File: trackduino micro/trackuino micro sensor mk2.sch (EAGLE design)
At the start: 42 parts, among them IC2 74AHC1G125DBV, SW1 SPST_TACT-KMR2, U1 ATMEGA168MLF, Y1 16MHZ

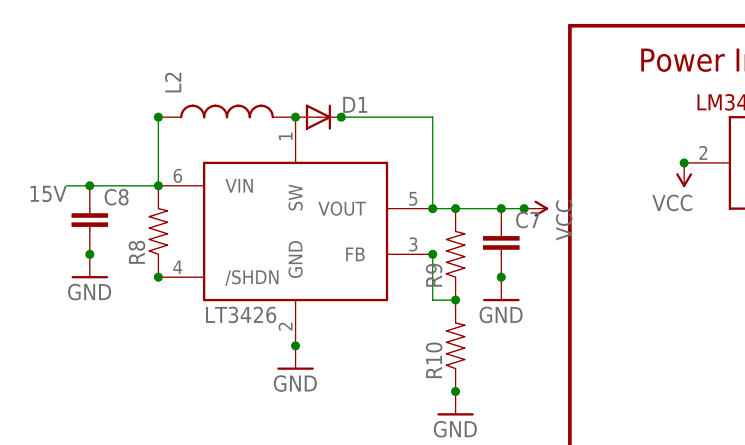
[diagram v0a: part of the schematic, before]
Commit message: sensor mk2 fixes
fixed a short on the boost output and serial RX
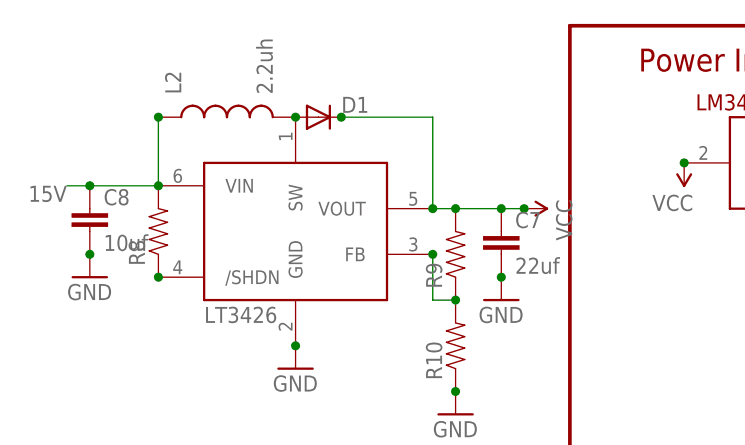
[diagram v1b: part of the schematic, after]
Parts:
- C7: value (none) -> 22uf
- C8: value (none) -> 10uf
- L2: value (none) -> 2.2uh
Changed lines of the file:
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@@
 <part name="U$7" library="adafruit" deviceset="LT3426" device=""/>
 <part name="D1" library="diode" deviceset="DIODE-" device="SOD123"/>
-<part name="L2" library="SparkFun-Passives" deviceset="INDUCTOR" device="0805"/>
+<part name="L2" library="SparkFun-Passives" deviceset="INDUCTOR" device="0805" value="2.2uh"/>
 <part name="R8" library="SparkFun-Resistors" deviceset="RESISTOR" device="0805-RES"/>
 <part name="R9" library="SparkFun-Resistors" deviceset="RESISTOR" device="0805-RES"/>
 <part name="R10" library="SparkFun-Resistors" deviceset="RESISTOR" device="0805-RES"/>
 <part name="GND28" library="SparkFun-Aesthetics" deviceset="GND" device=""/>
-<part name="C7" library="SparkFun-Capacitors" deviceset="CAP" device="0805"/>
-<part name="C8" library="SparkFun-Capacitors" deviceset="CAP" device="0805"/>
+<part name="C7" library="SparkFun-Capacitors" deviceset="CAP" device="0805" value="22uf"/>
+<part name="C8" library="SparkFun-Capacitors" deviceset="CAP" device="0805" value="10uf"/>
 <part name="GND29" library="SparkFun-Aesthetics" deviceset="GND" device=""/>
 <part name="GND30" library="SparkFun-Aesthetics" deviceset="GND" device=""/>

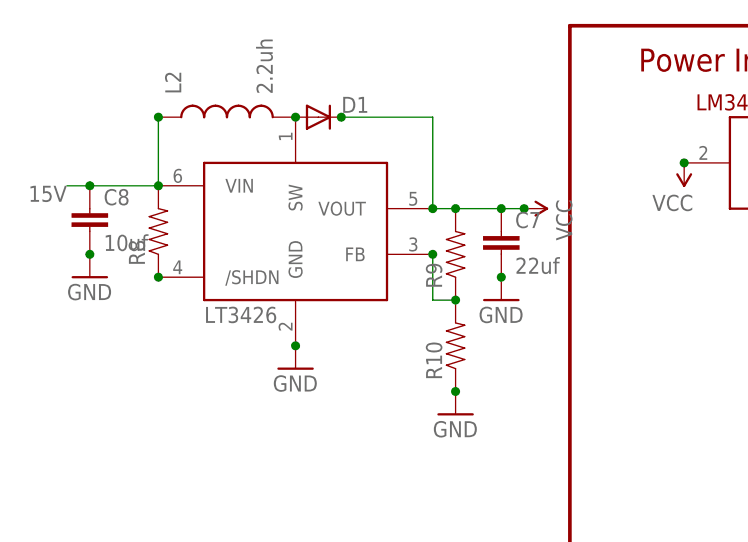
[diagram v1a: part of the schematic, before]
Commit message: DRC check
ran osh park DRC check and resolved errors.
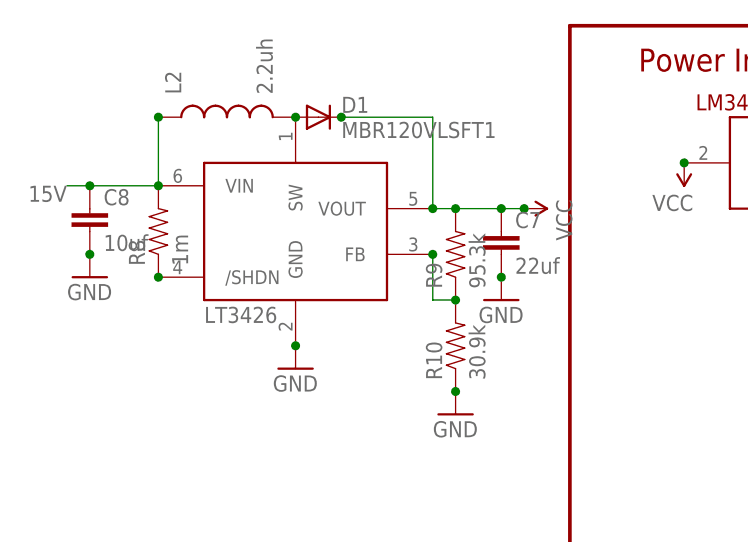
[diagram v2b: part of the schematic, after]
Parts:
- D1: value (none) -> MBR120VLSFT1
- R10: value (none) -> 30.9k
- R8: value (none) -> 1m
- R9: value (none) -> 95.3k
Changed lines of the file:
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@@
 <part name="SUPPLY1" library="SparkFun-Aesthetics" deviceset="VCC" device=""/>
 <part name="U$7" library="adafruit" deviceset="LT3426" device=""/>
-<part name="D1" library="diode" deviceset="DIODE-" device="SOD123"/>
+<part name="D1" library="diode" deviceset="DIODE-" device="SOD123" value="MBR120VLSFT1"/>
 <part name="L2" library="SparkFun-Passives" deviceset="INDUCTOR" device="0805" value="2.2uh"/>
-<part name="R8" library="SparkFun-Resistors" deviceset="RESISTOR" device="0805-RES"/>
-<part name="R9" library="SparkFun-Resistors" deviceset="RESISTOR" device="0805-RES"/>
-<part name="R10" library="SparkFun-Resistors" deviceset="RESISTOR" device="0805-RES"/>
+<part name="R8" library="SparkFun-Resistors" deviceset="RESISTOR" device="0805-RES" value="1m"/>
+<part name="R9" library="SparkFun-Resistors" deviceset="RESISTOR" device="0805-RES" value="95.3k"/>
+<part name="R10" library="SparkFun-Resistors" deviceset="RESISTOR" device="0805-RES" value="30.9k"/>
 <part name="GND28" library="SparkFun-Aesthetics" deviceset="GND" device=""/>
 <part name="C7" library="SparkFun-Capacitors" deviceset="CAP" device="0805" value="22uf"/>

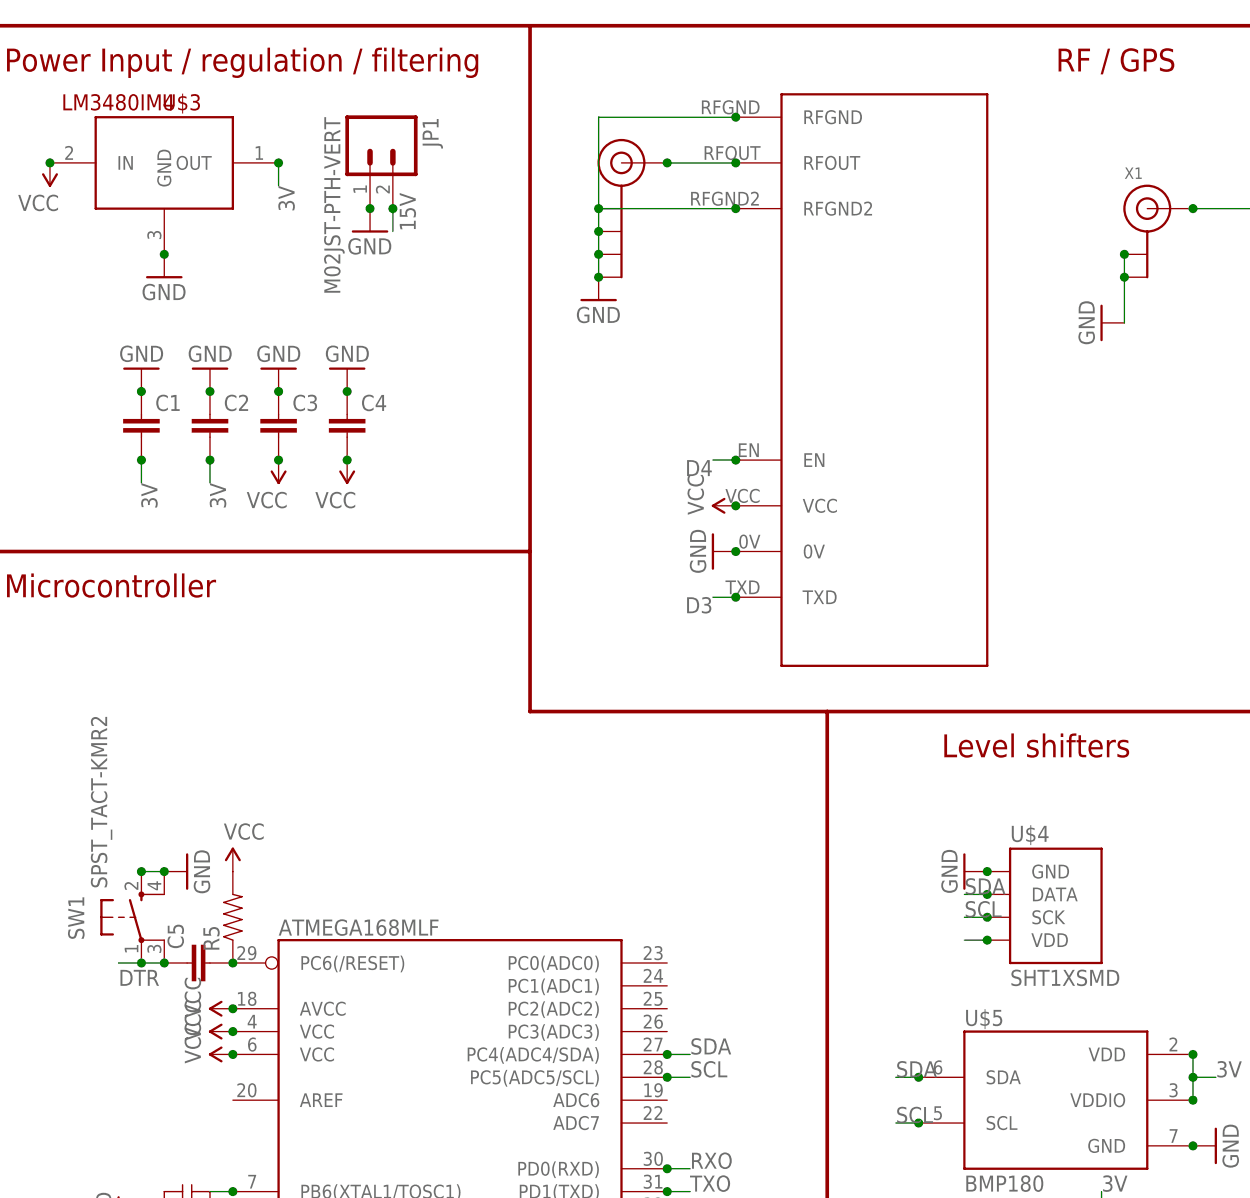
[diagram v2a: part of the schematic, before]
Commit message: boost converter fix
fixed external component placement and added some silkscreen
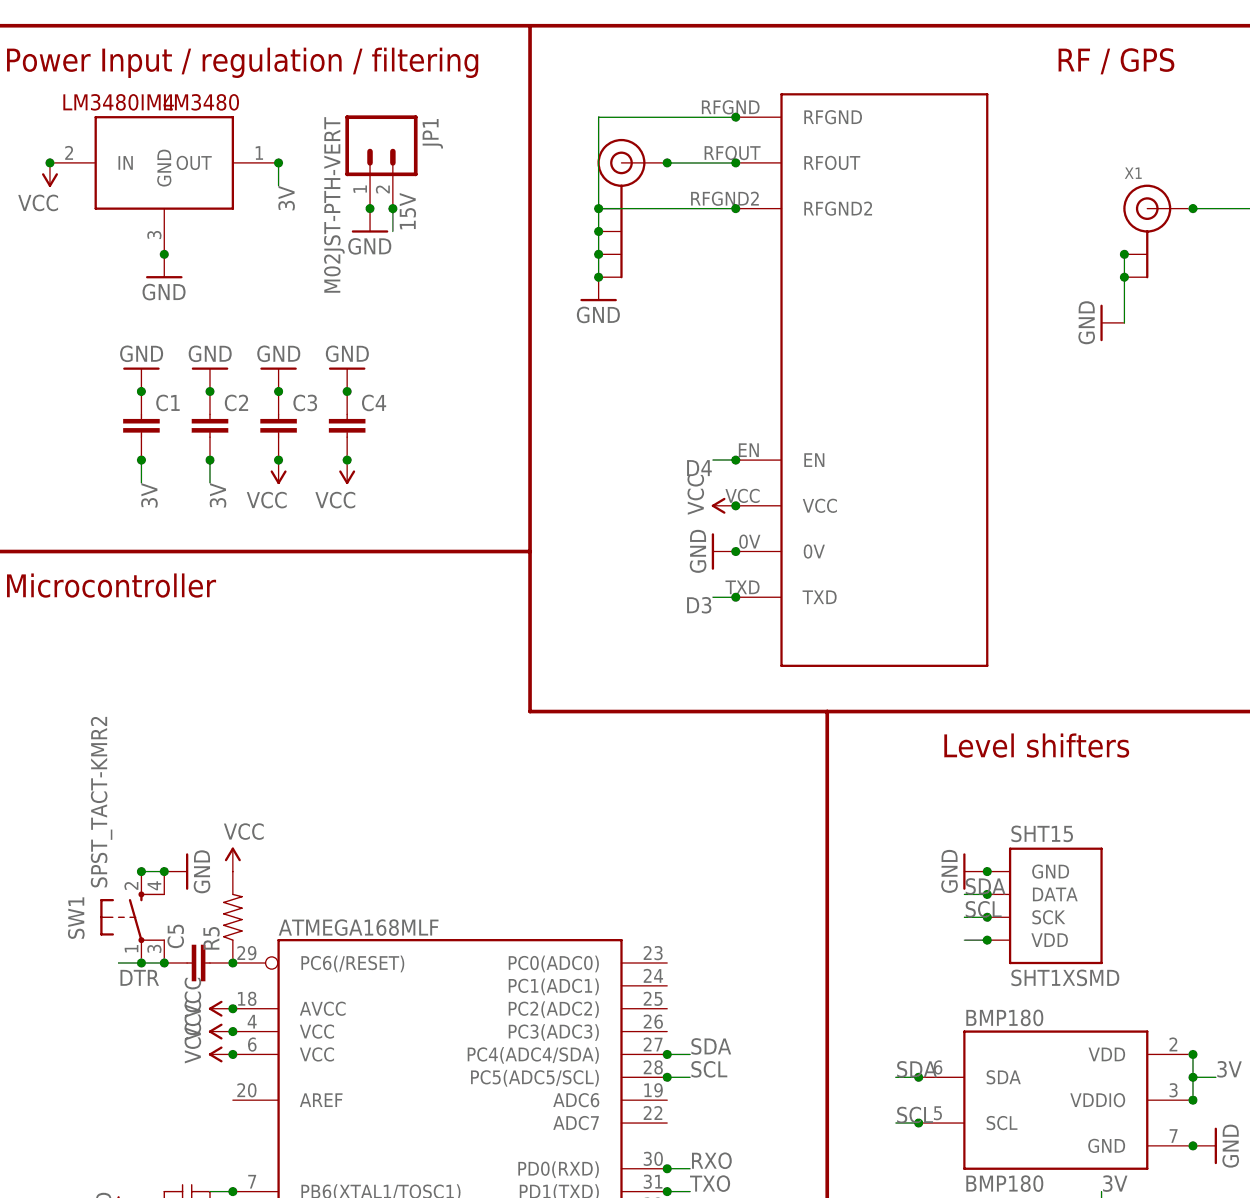
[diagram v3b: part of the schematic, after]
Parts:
- renumbered U$3 to LM3480, U$4 to SHT15, U$5 to BMP180, U$7 to LT3426
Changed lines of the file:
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@@
 <part name="U1" library="SparkFun-DigitalIC" deviceset="ATMEGA168" device="MLF" value="ATMEGA168MLF"/>
 <part name="U$2" library="Ava" deviceset="RADIOMETRIX-HX1" device=""/>
-<part name="U$3" library="SparkFun-PowerIC" deviceset="LM3480IM4" device=""/>
+<part name="LM3480" library="SparkFun-PowerIC" deviceset="LM3480IM4" device=""/>
 <part name="GND2" library="SparkFun-Aesthetics" deviceset="GND" device=""/>
 <part name="JP1" library="SparkFun-Connectors" deviceset="M02" device="JST-PTH-VERT" value="M02JST-PTH-VERT"/>
@@
 <part name="RX" library="SparkFun-Connectors" deviceset="M02" device="PTH" value="RX"/>
 <part name="GND10" library="SparkFun-Aesthetics" deviceset="GND" device=""/>
-<part name="U$4" library="SparkFun-Sensors" deviceset="SHT1X" device="SMD"/>
-<part name="U$5" library="SparkFun-Sensors" deviceset="BMP180" device=""/>
+<part name="SHT15" library="SparkFun-Sensors" deviceset="SHT1X" device="SMD"/>
+<part name="BMP180" library="SparkFun-Sensors" deviceset="BMP180" device=""/>
 <part name="GND16" library="SparkFun-Aesthetics" deviceset="GND" device=""/>
 <part name="GND20" library="SparkFun-Aesthetics" deviceset="GND" device=""/>
@@
 <part name="GND27" library="SparkFun-Aesthetics" deviceset="GND" device=""/>
 <part name="SUPPLY1" library="SparkFun-Aesthetics" deviceset="VCC" device=""/>
-<part name="U$7" library="adafruit" deviceset="LT3426" device=""/>
+<part name="LT3426" library="adafruit" deviceset="LT3426" device=""/>
 <part name="D1" library="diode" deviceset="DIODE-" device="SOD123" value="MBR120VLSFT1"/>
 <part name="L2" library="SparkFun-Passives" deviceset="INDUCTOR" device="0805" value="2.2uh"/>
@@
 <instance part="U1" gate="G$1" x="55.88" y="55.88"/>
 <instance part="U$2" gate="G$1" x="91.44" y="134.62" rot="R270"/>
-<instance part="U$3" gate="G$1" x="25.4" y="170.18"/>
+<instance part="LM3480" gate="G$1" x="25.4" y="170.18"/>
 <instance part="GND2" gate="1" x="114.3" y="43.18" rot="R270"/>
 <instance part="JP1" gate="G$1" x="48.26" y="172.72" rot="R270"/>
@@
 <instance part="RX" gate="G$1" x="231.14" y="83.82"/>
 <instance part="GND10" gate="1" x="208.28" y="58.42" rot="R90"/>
-<instance part="U$4" gate="G$1" x="124.46" y="86.36"/>
-<instance part="U$5" gate="G$1" x="124.46" y="66.04"/>
+<instance part="SHT15" gate="G$1" x="124.46" y="86.36"/>
+<instance part="BMP180" gate="G$1" x="124.46" y="66.04"/>
 <instance part="GND16" gate="1" x="142.24" y="60.96" rot="R90"/>
 <instance part="GND20" gate="1" x="114.3" y="91.44" rot="R270"/>
@@
 <instance part="GND27" gate="1" x="-30.48" y="147.32"/>
 <instance part="SUPPLY1" gate="G$1" x="-5.08" y="165.1" rot="R270"/>
-<instance part="U$7" gate="G$1" x="-30.48" y="162.56"/>
+<instance part="LT3426" gate="G$1" x="-30.48" y="162.56"/>
 <instance part="D1" gate="G$1" x="-27.94" y="175.26"/>
 <instance part="L2" gate="G$1" x="-38.1" y="175.26" rot="R90"/>
@@
 </segment>
 <segment>
-<pinref part="U$3" gate="G$1" pin="GND"/>
+<pinref part="LM3480" gate="G$1" pin="GND"/>
 <pinref part="GND3" gate="1" pin="GND"/>
 <junction x="25.4" y="160.02"/>
@@
 </segment>
 <segment>
-<pinref part="U$5" gate="G$1" pin="GND"/>
+<pinref part="BMP180" gate="G$1" pin="GND"/>
 <pinref part="GND16" gate="1" pin="GND"/>
 <junction x="139.7" y="60.96"/>
 </segment>
 <segment>
-<pinref part="U$4" gate="G$1" pin="GND"/>
+<pinref part="SHT15" gate="G$1" pin="GND"/>
 <pinref part="GND20" gate="1" pin="GND"/>
 <junction x="116.84" y="91.44"/>
 </segment>
 <segment>
-<pinref part="U$7" gate="G$1" pin="GND"/>
+<pinref part="LT3426" gate="G$1" pin="GND"/>
 <pinref part="GND27" gate="1" pin="GND"/>
 <junction x="-30.48" y="149.86"/>
@@
 <net name="VCC" class="0">
 <segment>
-<pinref part="U$3" gate="G$1" pin="IN"/>
+<pinref part="LM3480" gate="G$1" pin="IN"/>
 <pinref part="SUPPLY2" gate="G$1" pin="VCC"/>
 <junction x="12.7" y="170.18"/>
@@
 </segment>
 <segment>
-<pinref part="U$7" gate="G$1" pin="VOUT"/>
+<pinref part="LT3426" gate="G$1" pin="VOUT"/>
 <pinref part="SUPPLY1" gate="G$1" pin="VCC"/>
 <wire x1="-5.08" y1="165.1" x2="-7.62" y2="165.1" width="0.1524" layer="91"/>
@@
 <net name="3V" class="0">
 <segment>
-<pinref part="U$3" gate="G$1" pin="OUT"/>
+<pinref part="LM3480" gate="G$1" pin="OUT"/>
 <wire x1="38.1" y1="167.64" x2="38.1" y2="170.18" width="0.1524" layer="91"/>
 <label x="38.1" y="167.64" size="1.778" layer="95" rot="R270"/>
@@
 </segment>
 <segment>
-<pinref part="U$5" gate="G$1" pin="VDD"/>
-<pinref part="U$5" gate="G$1" pin="VDDIO"/>
+<pinref part="BMP180" gate="G$1" pin="VDD"/>
+<pinref part="BMP180" gate="G$1" pin="VDDIO"/>
 <wire x1="139.7" y1="71.12" x2="139.7" y2="68.58" width="0.1524" layer="91"/>
 <wire x1="139.7" y1="68.58" x2="139.7" y2="66.04" width="0.1524" layer="91"/>
@@
 </segment>
 <segment>
-<pinref part="U$4" gate="G$1" pin="VDD"/>
+<pinref part="SHT15" gate="G$1" pin="VDD"/>
 <wire x1="116.84" y1="83.82" x2="114.3" y2="83.82" width="0.1524" layer="91"/>
 <junction x="116.84" y="83.82"/>
@@
 </segment>
 <segment>
-<pinref part="U$4" gate="G$1" pin="DATA"/>
+<pinref part="SHT15" gate="G$1" pin="DATA"/>
 <wire x1="116.84" y1="88.9" x2="114.3" y2="88.9" width="0.1524" layer="91"/>
 <label x="114.3" y="88.9" size="1.778" layer="95"/>
@@
 </segment>
 <segment>
-<pinref part="U$5" gate="G$1" pin="SDA"/>
+<pinref part="BMP180" gate="G$1" pin="SDA"/>
 <wire x1="109.22" y1="68.58" x2="106.68" y2="68.58" width="0.1524" layer="91"/>
 <label x="106.68" y="68.58" size="1.778" layer="95"/>
@@
 </segment>
 <segment>
-<pinref part="U$4" gate="G$1" pin="SCK"/>
+<pinref part="SHT15" gate="G$1" pin="SCK"/>
 <wire x1="116.84" y1="86.36" x2="114.3" y2="86.36" width="0.1524" layer="91"/>
 <label x="114.3" y="86.36" size="1.778" layer="95"/>
@@
 </segment>
 <segment>
-<pinref part="U$5" gate="G$1" pin="SCL"/>
+<pinref part="BMP180" gate="G$1" pin="SCL"/>
 <wire x1="109.22" y1="63.5" x2="106.68" y2="63.5" width="0.1524" layer="91"/>
 <label x="106.68" y="63.5" size="1.778" layer="95"/>
@@
 <wire x1="-45.72" y1="167.64" x2="-53.34" y2="167.64" width="0.1524" layer="91"/>
 <label x="-55.88" y="167.64" size="1.778" layer="95" rot="R180"/>
-<pinref part="U$7" gate="G$1" pin="VIN"/>
+<pinref part="LT3426" gate="G$1" pin="VIN"/>
 <junction x="-45.72" y="167.64"/>
 <pinref part="L2" gate="G$1" pin="1"/>
@@
 <net name="N$9" class="0">
 <segment>
-<pinref part="U$7" gate="G$1" pin="SW"/>
+<pinref part="LT3426" gate="G$1" pin="SW"/>
 <pinref part="D1" gate="G$1" pin="A"/>
 <pinref part="L2" gate="G$1" pin="2"/>
@@
 <net name="N$12" class="0">
 <segment>
-<pinref part="U$7" gate="G$1" pin="/SHDN"/>
+<pinref part="LT3426" gate="G$1" pin="/SHDN"/>
 <pinref part="R8" gate="G$1" pin="1"/>
 <junction x="-45.72" y="157.48"/>
@@
 <pinref part="R9" gate="G$1" pin="1"/>
 <pinref part="R10" gate="G$1" pin="2"/>
-<pinref part="U$7" gate="G$1" pin="FB"/>
+<pinref part="LT3426" gate="G$1" pin="FB"/>
 <wire x1="-15.24" y1="160.02" x2="-15.24" y2="154.94" width="0.1524" layer="91"/>
 <wire x1="-15.24" y1="154.94" x2="-12.7" y2="154.94" width="0.1524" layer="91"/>
